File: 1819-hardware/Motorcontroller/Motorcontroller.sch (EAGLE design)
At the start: 31 parts, among them U1 GENERIC-SOIC8MSGEQ7N-FILTER, U2 GENERIC-SOIC8MSGEQ7N-FILTER, U3 GENERIC-SOIC8MSGEQ7N-FILTER, U4 PCA9685

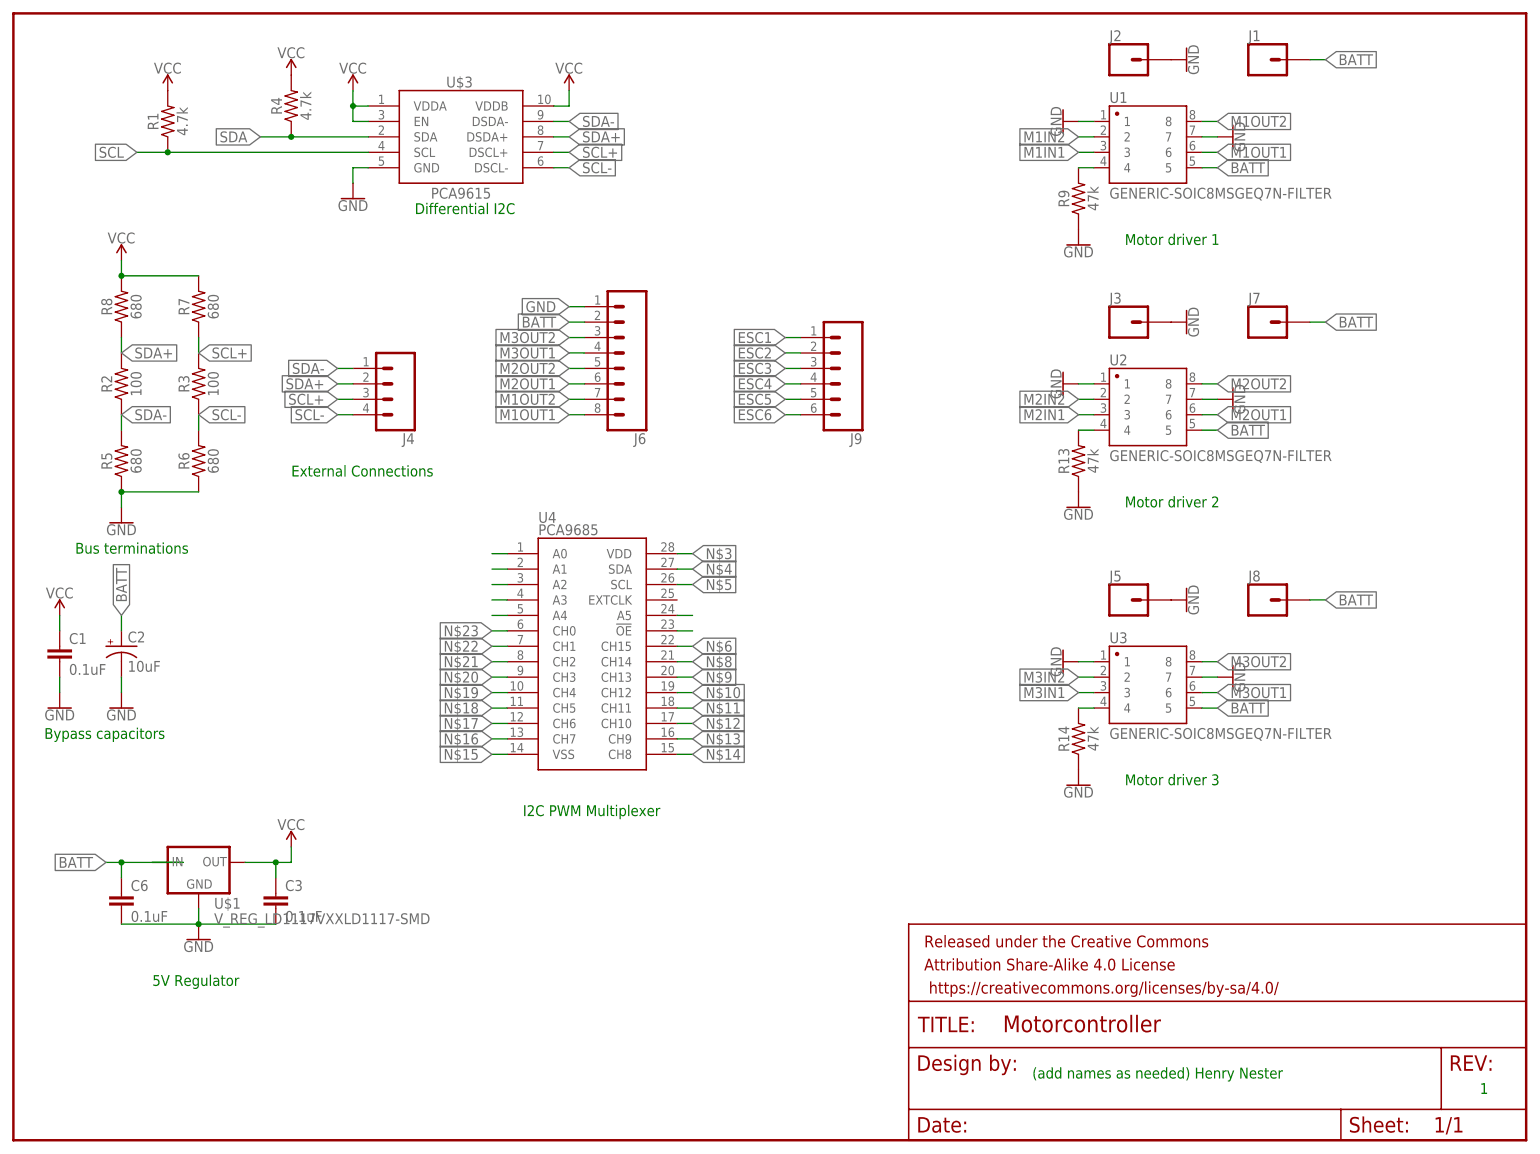
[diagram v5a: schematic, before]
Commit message: component positions done
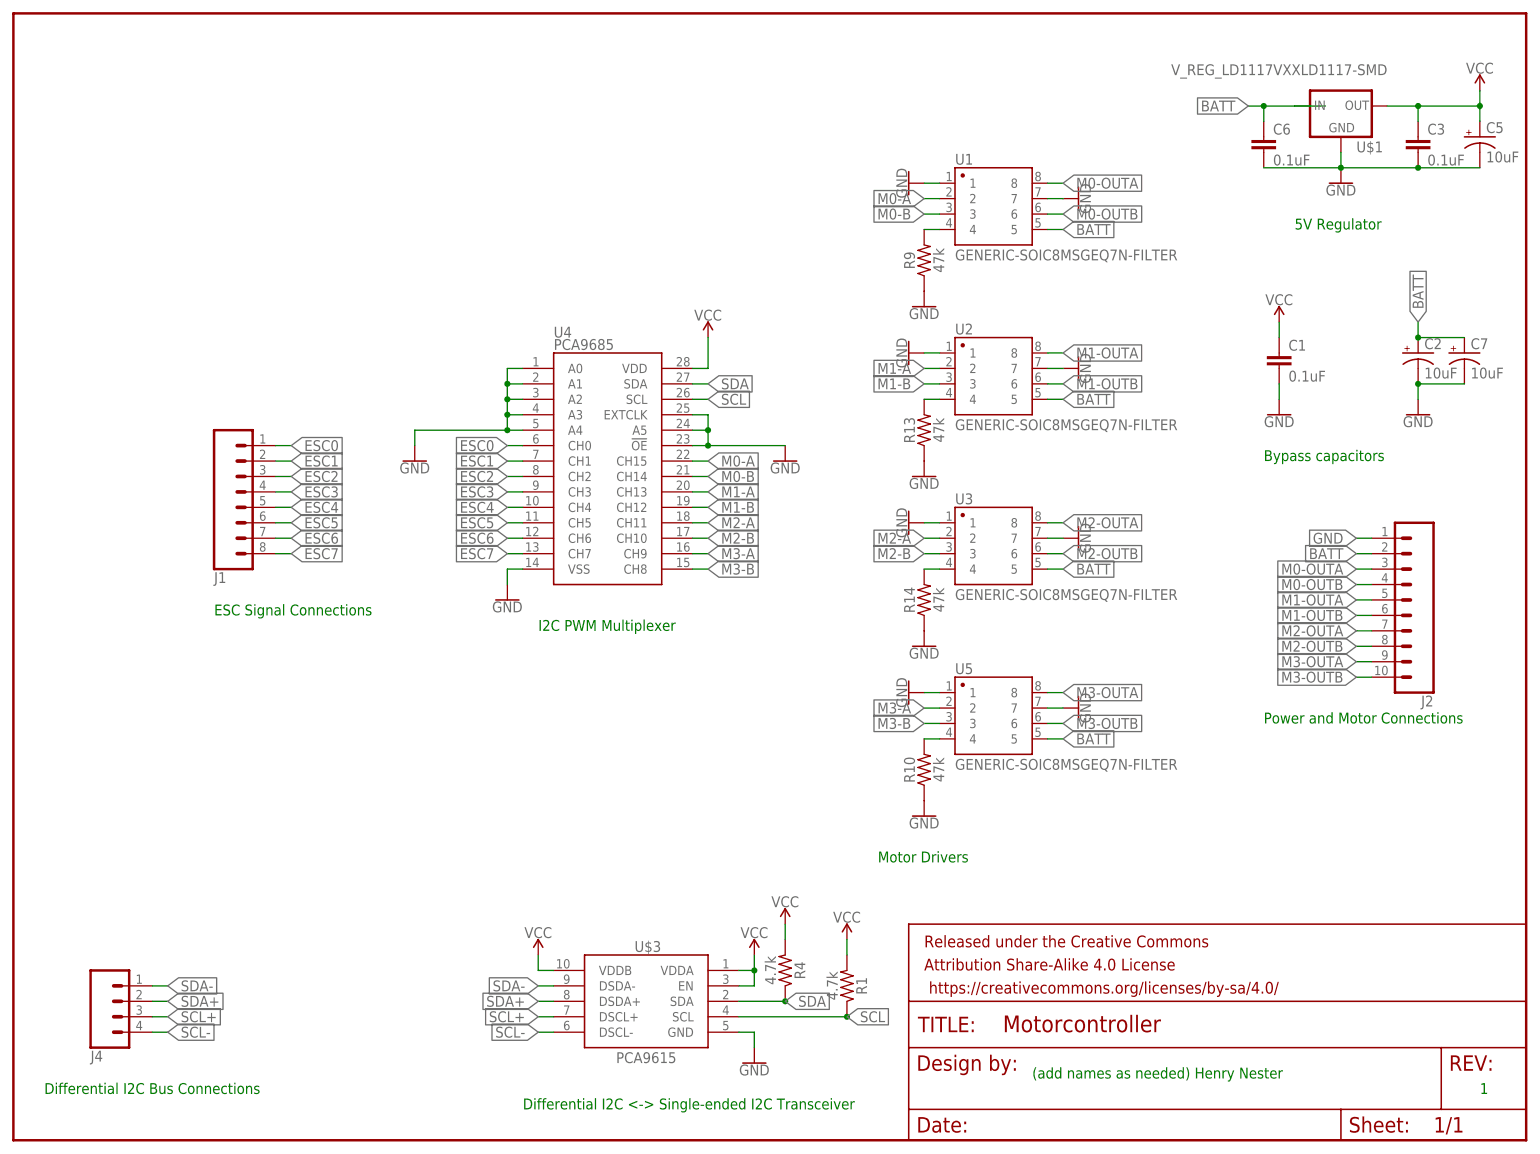
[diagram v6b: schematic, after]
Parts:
- removed J3, J5, J7, J8: (no value), SparkFun-Connectors:CONN_01PTH_NO_SILK_YES_STOP
- removed J6: (no value), SparkFun-Connectors:CONN_08LONGPADS
- removed J9: (no value), SparkFun-Connectors:CONN_06SILK_FEMALE_PTH
- removed R2, R3: 100, SparkFun-Resistors:100OHM-0603-1/4W-5%
- removed R5, R6, R7, R8: 680, SparkFun-Resistors:680OHM-0603-1/10W-5%
- added C5, C7: 10uF, SparkFun-Capacitors:10UF-POLAR-RADIAL-2.5MM-25V-20%
- added R10: 47k, SparkFun-Resistors:47KOHM-0603-1/10W-1%
- added U5: GENERIC-SOIC8MSGEQ7N-FILTER, SparkFun-Retired:GENERIC-SOIC8MSGEQ7N-FILTER
- J1: device SparkFun-Connectors:CONN_01PTH_NO_SILK_YES_STOP -> SparkFun-Connectors:CONN_08"
- J2: device SparkFun-Connectors:CONN_01PTH_NO_SILK_YES_STOP -> SparkFun-Connectors:CONN_10"
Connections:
- removed net M1IN1: U1.3
- removed net M1IN2: U1.2
- removed net M1OUT1: J6.8, U1.6
- removed net M1OUT2: J6.7, U1.8
- removed net M2IN1: U2.3
- removed net M2IN2: U2.2
- removed net M2OUT1: J6.6, U2.6
- removed net M2OUT2: J6.5, U2.8
- removed net M3IN1: U3.3
- removed net M3IN2: U3.2
- removed net M3OUT1: J6.4, U3.6
- removed net M3OUT2: J6.3, U3.8
- removed net N$10: U4.CH12
- removed net N$11: U4.CH11
- removed net N$12: U4.CH10
- removed net N$13: U4.CH9
- removed net N$14: U4.CH8
- removed net N$15: U4.VSS
- removed net N$16: U4.CH7
- removed net N$17: U4.CH6
- removed net N$18: U4.CH5
- removed net N$19: U4.CH4
- removed net N$20: U4.CH3
- removed net N$21: U4.CH2
- removed net N$22: U4.CH1
- removed net N$23: U4.CH0
- removed net N$24: U4.A4
- removed net N$25: U4.A3
- removed net N$26: U4.A2
- removed net N$27: U4.A1
- removed net N$28: U4.A0
- removed net N$29: U4.A5
- removed net N$30: U4.!OE
- removed net N$4: U4.SDA
- removed net N$5: U4.SCL
- removed net N$6: U4.CH15
- removed net N$8: U4.CH14
- removed net N$9: U4.CH13
- new net ESC0: J1.1, U4.CH0
- new net ESC7: J1.8, U4.CH7
- new net M0-A: U1.2, U4.CH15
- new net M0-B: U1.3, U4.CH14
- new net M0-OUTA: J2.3, U1.8
- new net M0-OUTB: J2.4, U1.6
- new net M1-A: U2.2, U4.CH13
- new net M1-B: U2.3, U4.CH12
- new net M1-OUTA: J2.5, U2.8
- new net M1-OUTB: J2.6, U2.6
- new net M2-A: U3.2, U4.CH11
- new net M2-B: U3.3, U4.CH10
- new net M2-OUTA: J2.7, U3.8
- new net M2-OUTB: J2.8, U3.6
- new net M3-A: U4.CH9, U5.2
- new net M3-B: U4.CH8, U5.3
- new net M3-OUTA: J2.9, U5.8
- new net M3-OUTB: J2.10, U5.6
- net BATT: now also C7.+, J2.2, U5.5; no longer J1.1, J6.2, J7.1, J8.1
- net ESC1: now also J1.2, U4.CH1; no longer J9.1
- net ESC2: now also J1.3, U4.CH2; no longer J9.2
- net ESC3: now also J1.4, U4.CH3; no longer J9.3
- net ESC4: now also J1.5, U4.CH4; no longer J9.4
- net ESC5: now also J1.6, U4.CH5; no longer J9.5
- net ESC6: now also J1.7, U4.CH6; no longer J9.6
- net GND: now also C5.-, C7.-, R10.1, U4.!OE, U4.A0, U4.A1, U4.A2, U4.A3, U4.A4, U4.A5, U4.EXTCLK, U4.VSS, U5.1, U5.7; no longer J3.1, J5.1, J6.1, R5.1, R6.1
- net N$3: now also R10.2, U5.4; no longer U4.VDD
- net SCL: now also U4.SCL
- net SCL+: no longer R3.2, R7.1
- net SCL-: no longer R3.1, R6.2
- net SDA: now also U4.SDA
- net SDA+: no longer R2.2, R8.1
- net SDA-: no longer R2.1, R5.2
- net VCC: now also C5.+, U4.VDD; no longer R7.2, R8.2
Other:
- note added: "Differential I2C <-> Single-ended I2C Transceiver"
- note added: "Differential I2C Bus Connections"
- note added: "ESC Signal Connections"
- note added: "Motor Drivers"
- note added: "Power and Motor Connections"
- note removed: "Bus terminations"
- note removed: "Differential I2C"
- note removed: "External Connections"
- note removed: "Motor driver 1"
- note removed: "Motor driver 2"
- note removed: "Motor driver 3"
- moved on the sheet: C1, C2, C3, C6, J4, R1, R13, R14, R4, R9, U$1, U$3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

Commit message: motorcontroller board
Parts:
- added J3, J5, J6, J7: (no value), SparkFun-Connectors:CONN_01PTH_NO_SILK_YES_STOP
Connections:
- net BATT: now also J2.10; no longer J2.2
- net GND: now also J3.1, J5.1, J6.1, J7.1
- net M0-OUTA: now also J2.2; no longer J2.3
- net M0-OUTB: now also J2.3; no longer J2.4
- net M1-OUTA: now also J2.4; no longer J2.5
- net M1-OUTB: now also J2.5; no longer J2.6
- net M2-OUTA: now also J2.6; no longer J2.7
- net M2-OUTB: now also J2.7; no longer J2.8
- net M3-OUTA: now also J2.8; no longer J2.9
- net M3-OUTB: now also J2.9; no longer J2.10
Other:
- note added: "For soldering heatsink pads"

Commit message: more work on boards
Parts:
- removed J2: (no value), SparkFun-Connectors:CONN_10"
- added J10, J9: (no value), SparkFun-Connectors:CONN_02
- added J11, J8: 455-1750-1-ND, SparkFun-Connectors:CONN_03
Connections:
- net BATT: now also J11.3; no longer J2.10
- net GND: now also J8.1; no longer J2.1
- net M0-OUTA: now also J8.2; no longer J2.2
- net M0-OUTB: now also J8.3; no longer J2.3
- net M1-OUTA: now also J9.1; no longer J2.4
- net M1-OUTB: now also J9.2; no longer J2.5
- net M2-OUTA: now also J10.1; no longer J2.6
- net M2-OUTB: now also J10.2; no longer J2.7
- net M3-OUTA: now also J11.1; no longer J2.8
- net M3-OUTB: now also J11.2; no longer J2.9
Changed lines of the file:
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@@
 <part name="R10" library="SparkFun-Resistors" library_urn="urn:adsk.eagle:library:532" deviceset="47KOHM" device="-0603-1/10W-1%" package3d_urn="urn:adsk.eagle:package:39650/1" value="47k"/>
 <part name="GND21" library="SparkFun-PowerSymbols" library_urn="urn:adsk.eagle:library:530" deviceset="GND" device=""/>
-<part name="J2" library="SparkFun-Connectors" deviceset="CONN_10" device="&quot;"/>
 <part name="J1" library="SparkFun-Connectors" deviceset="CONN_08" device="&quot;"/>
 <part name="C5" library="SparkFun-Capacitors" library_urn="urn:adsk.eagle:library:510" deviceset="10UF-POLAR" device="-RADIAL-2.5MM-25V-20%" package3d_urn="urn:adsk.eagle:package:37423/1" value="10uF"/>
@@
 <part name="GND22" library="SparkFun-PowerSymbols" deviceset="GND" device=""/>
 <part name="GND23" library="SparkFun-PowerSymbols" deviceset="GND" device=""/>
+<part name="J8" library="SparkFun-Connectors" deviceset="CONN_03" device="" value="455-1750-1-ND"/>
+<part name="J9" library="SparkFun-Connectors" deviceset="CONN_02" device=""/>
+<part name="J10" library="SparkFun-Connectors" deviceset="CONN_02" device=""/>
+<part name="J11" library="SparkFun-Connectors" deviceset="CONN_03" device="" value="455-1750-1-ND"/>
 </parts>
 <sheets>
@@
 <text x="241.3" y="7.62" size="1.778" layer="91">1</text>
 <text x="210.82" y="149.86" size="1.778" layer="91">5V Regulator</text>
-<text x="205.74" y="68.58" size="1.778" layer="91">Power and Motor Connections</text>
+<text x="205.74" y="58.42" size="1.778" layer="91">Power and Motor Connections</text>
 <text x="205.74" y="111.76" size="1.778" layer="91">Bypass capacitors</text>
 <text x="86.36" y="83.82" size="1.778" layer="91">I2C PWM Multiplexer</text>
@@
 <attribute name="VALUE" x="149.86" y="53.086" size="1.778" layer="96" align="top-center"/>
 </instance>
-<instance part="J2" gate="J1" x="233.68" y="81.28" rot="R180">
-<attribute name="VALUE" x="233.68" y="103.886" size="1.778" layer="96" font="vector" rot="R180"/>
-<attribute name="NAME" x="233.68" y="73.152" size="1.778" layer="95" font="vector" rot="R180"/>
-</instance>
 <instance part="J1" gate="G$1" x="38.1" y="106.68" rot="MR180">
 <attribute name="VALUE" x="33.02" y="119.126" size="1.778" layer="96" font="vector" rot="MR180"/>
@@
 <instance part="GND23" gate="1" x="139.7" y="167.64">
 <attribute name="VALUE" x="139.7" y="167.386" size="1.778" layer="96" align="top-center"/>
+</instance>
+<instance part="J8" gate="J$1" x="231.14" y="101.6" rot="R180">
+<attribute name="VALUE" x="233.68" y="108.966" size="1.778" layer="96" font="vector" rot="R180"/>
+<attribute name="NAME" x="233.68" y="96.012" size="1.778" layer="95" font="vector" rot="R180"/>
+</instance>
+<instance part="J9" gate="G$1" x="231.14" y="91.44" rot="R180">
+<attribute name="VALUE" x="233.68" y="96.266" size="1.778" layer="96" font="vector" rot="R180"/>
+<attribute name="NAME" x="233.68" y="80.772" size="1.778" layer="95" font="vector" rot="R180"/>
+</instance>
+<instance part="J10" gate="G$1" x="231.14" y="81.28" rot="R180">
+<attribute name="VALUE" x="233.68" y="86.106" size="1.778" layer="96" font="vector" rot="R180"/>
+<attribute name="NAME" x="233.68" y="65.532" size="1.778" layer="95" font="vector" rot="R180"/>
+</instance>
+<instance part="J11" gate="J$1" x="231.14" y="68.58" rot="R180">
+<attribute name="VALUE" x="233.68" y="75.946" size="1.778" layer="96" font="vector" rot="R180"/>
+<attribute name="NAME" x="233.68" y="62.992" size="1.778" layer="95" font="vector" rot="R180"/>
 </instance>
 </instances>
@@
 </segment>
 <segment>
-<wire x1="223.52" y1="99.06" x2="220.98" y2="99.06" width="0.1524" layer="91"/>
-<label x="220.98" y="99.06" size="1.778" layer="95" rot="R180" xref="yes"/>
-<pinref part="J2" gate="J1" pin="1"/>
+<wire x1="223.52" y1="104.14" x2="220.98" y2="104.14" width="0.1524" layer="91"/>
+<label x="220.98" y="104.14" size="1.778" layer="95" rot="R180" xref="yes"/>
+<pinref part="J8" gate="J$1" pin="1"/>
 </segment>
 <segment>
@@
 </segment>
 <segment>
-<pinref part="J2" gate="J1" pin="10"/>
-<wire x1="223.52" y1="76.2" x2="220.98" y2="76.2" width="0.1524" layer="91"/>
-<label x="220.98" y="76.2" size="1.778" layer="95" rot="R180" xref="yes"/>
+<wire x1="223.52" y1="66.04" x2="220.98" y2="66.04" width="0.1524" layer="91"/>
+<label x="220.98" y="66.04" size="1.778" layer="95" rot="R180" xref="yes"/>
+<pinref part="J11" gate="J$1" pin="3"/>
 </segment>
 </net>
@@
 </segment>
 <segment>
-<wire x1="223.52" y1="86.36" x2="220.98" y2="86.36" width="0.1524" layer="91"/>
-<label x="220.98" y="86.36" size="1.778" layer="95" rot="R180" xref="yes"/>
-<pinref part="J2" gate="J1" pin="6"/>
+<wire x1="223.52" y1="81.28" x2="220.98" y2="81.28" width="0.1524" layer="91"/>
+<label x="220.98" y="81.28" size="1.778" layer="95" rot="R180" xref="yes"/>
+<pinref part="J10" gate="G$1" pin="1"/>
 </segment>
 </net>
@@
 </segment>
 <segment>
-<wire x1="223.52" y1="83.82" x2="220.98" y2="83.82" width="0.1524" layer="91"/>
-<label x="220.98" y="83.82" size="1.778" layer="95" rot="R180" xref="yes"/>
-<pinref part="J2" gate="J1" pin="7"/>
+<wire x1="223.52" y1="78.74" x2="220.98" y2="78.74" width="0.1524" layer="91"/>
+<label x="220.98" y="78.74" size="1.778" layer="95" rot="R180" xref="yes"/>
+<pinref part="J10" gate="G$1" pin="2"/>
 </segment>
 </net>
@@
 <wire x1="223.52" y1="91.44" x2="220.98" y2="91.44" width="0.1524" layer="91"/>
 <label x="220.98" y="91.44" size="1.778" layer="95" rot="R180" xref="yes"/>
-<pinref part="J2" gate="J1" pin="4"/>
+<pinref part="J9" gate="G$1" pin="1"/>
 </segment>
 </net>
@@
 <wire x1="223.52" y1="88.9" x2="220.98" y2="88.9" width="0.1524" layer="91"/>
 <label x="220.98" y="88.9" size="1.778" layer="95" rot="R180" xref="yes"/>
-<pinref part="J2" gate="J1" pin="5"/>
+<pinref part="J9" gate="G$1" pin="2"/>
 </segment>
 </net>
@@
 </segment>
 <segment>
-<wire x1="223.52" y1="96.52" x2="220.98" y2="96.52" width="0.1524" layer="91"/>
-<label x="220.98" y="96.52" size="1.778" layer="95" rot="R180" xref="yes"/>
-<pinref part="J2" gate="J1" pin="2"/>
+<wire x1="223.52" y1="101.6" x2="220.98" y2="101.6" width="0.1524" layer="91"/>
+<label x="220.98" y="101.6" size="1.778" layer="95" rot="R180" xref="yes"/>
+<pinref part="J8" gate="J$1" pin="2"/>
 </segment>
 </net>
@@
 </segment>
 <segment>
-<wire x1="223.52" y1="93.98" x2="220.98" y2="93.98" width="0.1524" layer="91"/>
-<label x="220.98" y="93.98" size="1.778" layer="95" rot="R180" xref="yes"/>
-<pinref part="J2" gate="J1" pin="3"/>
+<wire x1="223.52" y1="99.06" x2="220.98" y2="99.06" width="0.1524" layer="91"/>
+<label x="220.98" y="99.06" size="1.778" layer="95" rot="R180" xref="yes"/>
+<pinref part="J8" gate="J$1" pin="3"/>
 </segment>
 </net>
@@
 </segment>
 <segment>
-<wire x1="223.52" y1="81.28" x2="220.98" y2="81.28" width="0.1524" layer="91"/>
-<label x="220.98" y="81.28" size="1.778" layer="95" rot="R180" xref="yes"/>
-<pinref part="J2" gate="J1" pin="8"/>
+<wire x1="223.52" y1="71.12" x2="220.98" y2="71.12" width="0.1524" layer="91"/>
+<label x="220.98" y="71.12" size="1.778" layer="95" rot="R180" xref="yes"/>
+<pinref part="J11" gate="J$1" pin="1"/>
 </segment>
 </net>
@@
 </segment>
 <segment>
-<pinref part="J2" gate="J1" pin="9"/>
-<wire x1="223.52" y1="78.74" x2="220.98" y2="78.74" width="0.1524" layer="91"/>
-<label x="220.98" y="78.74" size="1.778" layer="95" rot="R180" xref="yes"/>
-</segment>
-</net>
+<wire x1="223.52" y1="68.58" x2="220.98" y2="68.58" width="0.1524" layer="91"/>
+<label x="220.98" y="68.58" size="1.778" layer="95" rot="R180" xref="yes"/>
+<pinref part="J11" gate="J$1" pin="2"/>
+</segment>
+</net>
